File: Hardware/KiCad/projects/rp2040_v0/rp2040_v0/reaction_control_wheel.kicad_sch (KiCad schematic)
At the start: 13 parts, among them J16 Conn_01x03, J22 Conn_02x05_Odd_Even, J23 Screw_Terminal_01x02, U12 DRV8837

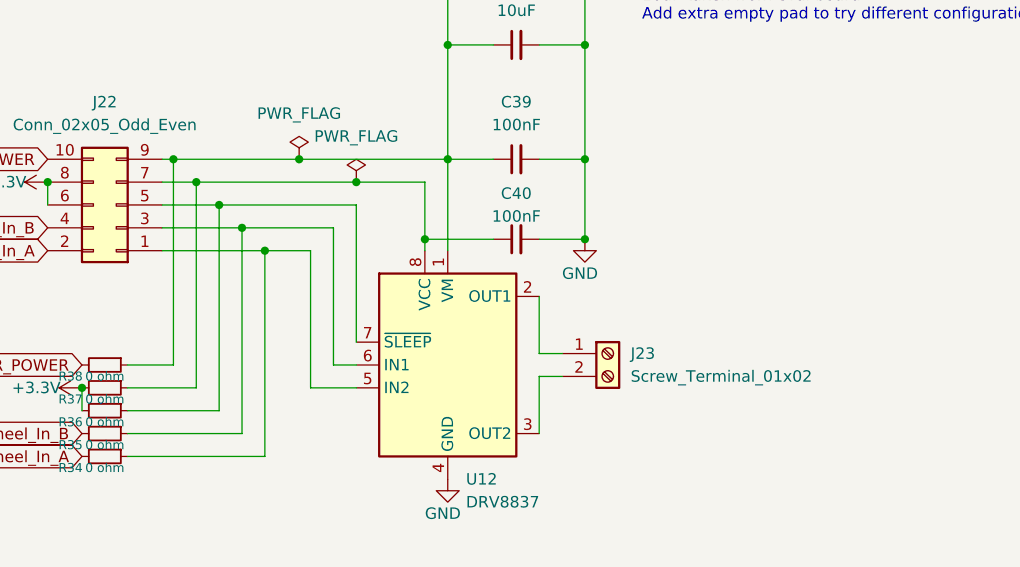
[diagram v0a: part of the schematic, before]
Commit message: Rev 0 ready to ship! Had to move IMU so board got sloppy. IMU should be in the middle of the board. Glad I caught that.
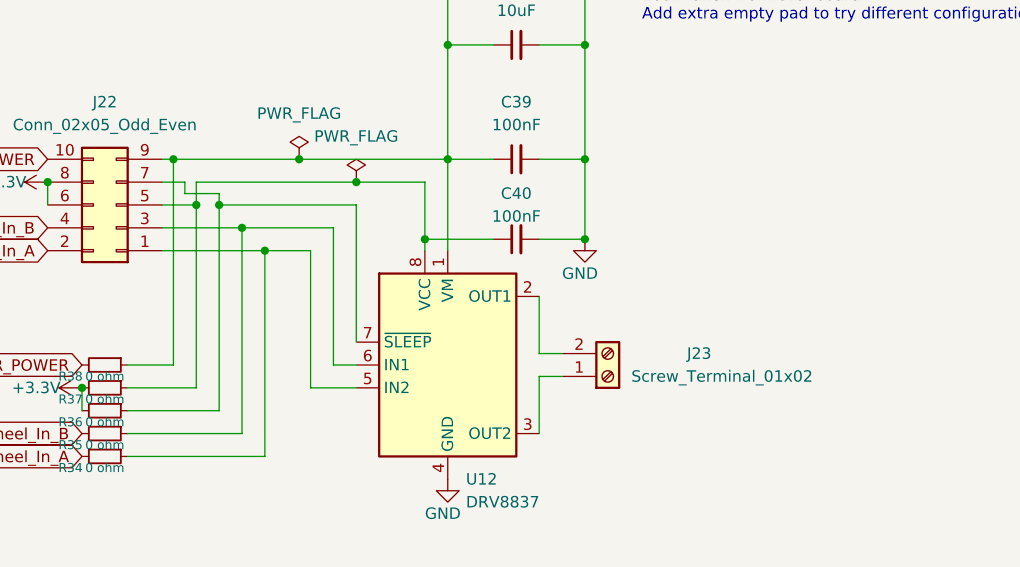
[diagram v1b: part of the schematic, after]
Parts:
- C38: JLC Part (none) -> Basic Part; LCSC Part (none) -> C15850
- C39, C40: JLC Part (none) -> Basic Part; LCSC Part (none) -> C307331
- J23: JLC Part (none) -> DNP; LCSC Part (none) -> C557651
- R34, R35, R36, R37, R38: JLC Part (none) -> Basic Part; LCSC Part (none) -> C17168
- U12: JLC Part (none) -> Extended Part; LCSC Part (none) -> C39159
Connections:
- net at R36.1, U12.7 (~{SLEEP}): now also J22.7 (Pin_7); no longer J22.5 (Pin_5)
- net at C40.1, R37.1, U12.8 (VCC): now also J22.5 (Pin_5); no longer J22.7 (Pin_7)
- net at J23.1 (Pin_1): now also U12.3 (OUT2); no longer U12.2 (OUT1)
- net at J23.2 (Pin_2): now also U12.2 (OUT1); no longer U12.3 (OUT2)
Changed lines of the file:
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@@
   (junction (at 147.32 93.98) (diameter 0) (color 0 0 0 0)
   )
-  (junction (at 142.24 88.9) (diameter 0) (color 0 0 0 0)
+  (junction (at 142.24 91.44) (diameter 0) (color 0 0 0 0)
   )
   (junction (at 129.54 111.76) (diameter 0) (color 0 0 0 0)
@@
   (junction (at 167.64 95.25) (diameter 0) (color 0 0 0 0)
   )
+  (junction (at 160.02 88.9) (diameter 0) (color 0 0 0 0)
+  )
+  (junction (at 185.42 73.66) (diameter 0) (color 0 0 0 0)
+  )
+  (junction (at 170.18 73.66) (diameter 0) (color 0 0 0 0)
+  )
   (junction (at 144.78 91.44) (diameter 0) (color 0 0 0 0)
   )
-  (junction (at 160.02 88.9) (diameter 0) (color 0 0 0 0)
-  )
-  (junction (at 185.42 73.66) (diameter 0) (color 0 0 0 0)
-  )
-  (junction (at 170.18 73.66) (diameter 0) (color 0 0 0 0)
-  )
   (wire (pts (xy 180.34 110.49) (xy 180.34 116.84))
     (stroke (width 0) (type default) (color 0 0 0 0))
@@
     (stroke (width 0) (type default) (color 0 0 0 0))
   )
+  (wire (pts (xy 138.43 91.44) (xy 142.24 91.44))
+    (stroke (width 0) (type default) (color 0 0 0 0))
+  )
   (wire (pts (xy 182.88 107.95) (xy 180.34 107.95))
     (stroke (width 0) (type default) (color 0 0 0 0))
@@
     (stroke (width 0) (type default) (color 0 0 0 0))
   )
-  (wire (pts (xy 142.24 88.9) (xy 138.43 88.9))
-    (stroke (width 0) (type default) (color 0 0 0 0))
-  )
   (polyline (pts (xy 246.38 53.34) (xy 246.38 151.13))
     (stroke (width 0) (type default) (color 0 0 0 0))
@@
     (stroke (width 0) (type default) (color 0 0 0 0))
   )
-  (wire (pts (xy 144.78 91.44) (xy 138.43 91.44))
+  (wire (pts (xy 138.43 88.9) (xy 140.97 88.9))
+    (stroke (width 0) (type default) (color 0 0 0 0))
+  )
+  (wire (pts (xy 142.24 91.44) (xy 142.24 111.76))
     (stroke (width 0) (type default) (color 0 0 0 0))
   )
@@
     (stroke (width 0) (type default) (color 0 0 0 0))
   )
+  (wire (pts (xy 140.97 88.9) (xy 140.97 90.17))
+    (stroke (width 0) (type default) (color 0 0 0 0))
+  )
+  (wire (pts (xy 140.97 90.17) (xy 144.78 90.17))
+    (stroke (width 0) (type default) (color 0 0 0 0))
+  )
   (wire (pts (xy 185.42 62.23) (xy 185.42 73.66))
     (stroke (width 0) (type default) (color 0 0 0 0))
@@
     (stroke (width 0) (type default) (color 0 0 0 0))
   )
-  (wire (pts (xy 142.24 88.9) (xy 142.24 111.76))
+  (wire (pts (xy 142.24 88.9) (xy 142.24 91.44))
     (stroke (width 0) (type default) (color 0 0 0 0))
   )
@@
   )
   (polyline (pts (xy 45.72 53.34) (xy 45.72 151.13))
+    (stroke (width 0) (type default) (color 0 0 0 0))
+  )
+  (wire (pts (xy 144.78 90.17) (xy 144.78 91.44))
     (stroke (width 0) (type default) (color 0 0 0 0))
   )
@@
     )
     (property "Datasheet" "~" (id 3) (at 132.08 119.38 0)
+      (effects (font (size 1.27 1.27)) hide)
+    )
+    (property "LCSC Part" "C17168" (id 4) (at 132.08 119.38 0)
+      (effects (font (size 1.27 1.27)) hide)
+    )
+    (property "JLC Part" "Basic Part" (id 5) (at 132.08 119.38 0)
       (effects (font (size 1.27 1.27)) hide)
     )
@@
       (effects (font (size 1.27 1.27)) hide)
     )
+    (property "LCSC Part" "C15850" (id 4) (at 177.8 73.66 0)
+      (effects (font (size 1.27 1.27)) hide)
+    )
+    (property "JLC Part" "Basic Part" (id 5) (at 177.8 73.66 0)
+      (effects (font (size 1.27 1.27)) hide)
+    )
     (pin "1")
     (pin "2")
@@
     (pin "1")
   )
-  (symbol (lib_id "Connector:Screw_Terminal_01x02") (at 187.96 107.95 0) (unit 1)
-    (in_bom yes) (on_board yes) (fields_autoplaced)
-    (property "Reference" "J23" (id 0) (at 190.5 107.9499 0)
-      (effects (font (size 1.27 1.27)) (justify left))
-    )
-    (property "Value" "Screw_Terminal_01x02" (id 1) (at 190.5 110.4899 0)
-      (effects (font (size 1.27 1.27)) (justify left))
-    )
-    (property "Footprint" "easyeda2kicad:CONN-TH_XY301V-A-5.0-2P" (id 2) (at 187.96 107.95 0)
-      (effects (font (size 1.27 1.27)) hide)
-    )
-    (property "Datasheet" "~" (id 3) (at 187.96 107.95 0)
+  (symbol (lib_id "Connector:Screw_Terminal_01x02") (at 187.96 110.49 0) (mirror x) (unit 1)
+    (in_bom yes) (on_board yes)
+    (property "Reference" "J23" (id 0) (at 198.12 107.95 0))
+    (property "Value" "Screw_Terminal_01x02" (id 1) (at 200.66 110.49 0))
+    (property "Footprint" "easyeda2kicad:CONN-TH_XY301V-A-5.0-2P" (id 2) (at 187.96 110.49 0)
+      (effects (font (size 1.27 1.27)) hide)
+    )
+    (property "Datasheet" "~" (id 3) (at 187.96 110.49 0)
+      (effects (font (size 1.27 1.27)) hide)
+    )
+    (property "JLC Part" "DNP" (id 4) (at 187.96 110.49 0)
+      (effects (font (size 1.27 1.27)) hide)
+    )
+    (property "LCSC Part" "C557651" (id 5) (at 187.96 110.49 0)
       (effects (font (size 1.27 1.27)) hide)
     )
@@
       (effects (font (size 1.27 1.27)) hide)
     )
+    (property "LCSC Part" "C307331" (id 4) (at 177.8 86.36 0)
+      (effects (font (size 1.27 1.27)) hide)
+    )
+    (property "JLC Part" "Basic Part" (id 5) (at 177.8 86.36 0)
+      (effects (font (size 1.27 1.27)) hide)
+    )
     (pin "1")
     (pin "2")
@@
       (effects (font (size 1.27 1.27)) hide)
     )
+    (property "LCSC Part" "C17168" (id 4) (at 132.08 111.76 0)
+      (effects (font (size 1.27 1.27)) hide)
+    )
+    (property "JLC Part" "Basic Part" (id 5) (at 132.08 111.76 0)
+      (effects (font (size 1.27 1.27)) hide)
+    )
     (pin "1")
     (pin "2")
@@
       (effects (font (size 1.27 1.27)) hide)
     )
+    (property "LCSC Part" "C17168" (id 4) (at 132.08 114.3 0)
+      (effects (font (size 1.27 1.27)) hide)
+    )
+    (property "JLC Part" "Basic Part" (id 5) (at 132.08 114.3 0)
+      (effects (font (size 1.27 1.27)) hide)
+    )
     (pin "1")
     (pin "2")
@@
       (effects (font (size 1.27 1.27)) hide)
     )
+    (property "LCSC Part" "C17168" (id 4) (at 132.08 116.84 0)
+      (effects (font (size 1.27 1.27)) hide)
+    )
+    (property "JLC Part" "Basic Part" (id 5) (at 132.08 116.84 0)
+      (effects (font (size 1.27 1.27)) hide)
+    )
     (pin "1")
     (pin "2")
@@
     )
     (property "Datasheet" "http://www.ti.com/lit/ds/symlink/drv8837.pdf" (id 3) (at 170.18 109.22 0)
+      (effects (font (size 1.27 1.27)) hide)
+    )
+    (property "LCSC Part" "C39159" (id 4) (at 170.18 109.22 0)
+      (effects (font (size 1.27 1.27)) hide)
+    )
+    (property "JLC Part" "Extended Part" (id 5) (at 170.18 109.22 0)
       (effects (font (size 1.27 1.27)) hide)
     )
@@
       (effects (font (size 1.27 1.27)) hide)
     )
+    (property "LCSC Part" "C307331" (id 4) (at 177.8 95.25 0)
+      (effects (font (size 1.27 1.27)) hide)
+    )
+    (property "JLC Part" "Basic Part" (id 5) (at 177.8 95.25 0)
+      (effects (font (size 1.27 1.27)) hide)
+    )
     (pin "1")
     (pin "2")
@@
       (effects (font (size 1.27 1.27)) hide)
     )
+    (property "LCSC Part" "C17168" (id 4) (at 132.08 109.22 0)
+      (effects (font (size 1.27 1.27)) hide)
+    )
+    (property "JLC Part" "Basic Part" (id 5) (at 132.08 109.22 0)
+      (effects (font (size 1.27 1.27)) hide)
+    )

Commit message: Some minor changes with footprint. Sent to JLCPCB. Official Rev 0!
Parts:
- C38: LCSC (none) -> C15850
- C39, C40: LCSC (none) -> C307331
- J23: JLC Part DNP -> Extended Part; LCSC (none) -> C557651
- R34, R35, R36, R37, R38: LCSC (none) -> C17168
- U12: LCSC (none) -> C39159
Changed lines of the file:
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@@
+      (effects (font (size 1.27 1.27)) hide)
+    )
+    (property "LCSC" "C17168" (id 6) (at 132.08 119.38 0)
       (effects (font (size 1.27 1.27)) hide)
     )
@@
       (effects (font (size 1.27 1.27)) hide)
     )
+    (property "LCSC" "C15850" (id 6) (at 177.8 73.66 0)
+      (effects (font (size 1.27 1.27)) hide)
+    )
     (pin "1")
     (pin "2")
@@
       (effects (font (size 1.27 1.27)) hide)
     )
-    (property "JLC Part" "DNP" (id 4) (at 187.96 110.49 0)
+    (property "JLC Part" "Extended Part" (id 4) (at 187.96 110.49 0)
       (effects (font (size 1.27 1.27)) hide)
     )
     (property "LCSC Part" "C557651" (id 5) (at 187.96 110.49 0)
+      (effects (font (size 1.27 1.27)) hide)
+    )
+    (property "LCSC" "C557651" (id 6) (at 187.96 110.49 0)
       (effects (font (size 1.27 1.27)) hide)
     )
@@
       (effects (font (size 1.27 1.27)) hide)
     )
+    (property "LCSC" "C307331" (id 6) (at 177.8 86.36 0)
+      (effects (font (size 1.27 1.27)) hide)
+    )
     (pin "1")
     (pin "2")
@@
     )
     (property "JLC Part" "Basic Part" (id 5) (at 132.08 111.76 0)
+      (effects (font (size 1.27 1.27)) hide)
+    )
+    (property "LCSC" "C17168" (id 6) (at 132.08 111.76 0)
       (effects (font (size 1.27 1.27)) hide)
     )
@@
       (effects (font (size 1.27 1.27)) hide)
     )
+    (property "LCSC" "C17168" (id 6) (at 132.08 114.3 0)
+      (effects (font (size 1.27 1.27)) hide)
+    )
     (pin "1")
     (pin "2")
@@
       (effects (font (size 1.27 1.27)) hide)
     )
+    (property "LCSC" "C17168" (id 6) (at 132.08 116.84 0)
+      (effects (font (size 1.27 1.27)) hide)
+    )
     (pin "1")
     (pin "2")
@@
     )
     (property "JLC Part" "Extended Part" (id 5) (at 170.18 109.22 0)
+      (effects (font (size 1.27 1.27)) hide)
+    )
+    (property "LCSC" "C39159" (id 6) (at 170.18 109.22 0)
       (effects (font (size 1.27 1.27)) hide)
     )
@@
       (effects (font (size 1.27 1.27)) hide)
     )
+    (property "LCSC" "C307331" (id 6) (at 177.8 95.25 0)
+      (effects (font (size 1.27 1.27)) hide)
+    )
     (pin "1")
     (pin "2")
@@
       (effects (font (size 1.27 1.27)) hide)
     )
+    (property "LCSC" "C17168" (id 6) (at 132.08 109.22 0)
+      (effects (font (size 1.27 1.27)) hide)
+    )
